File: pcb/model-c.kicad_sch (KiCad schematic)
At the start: 107 parts, among them IC1 HT16K33, IC2 HT16K33, J1 Batt, J2 Conn_01x02_Socket, SW1 SW_SPST, SW10 SW_SPST, SW11 SW_SPST, SW12 SW_SPST, SW13 SW_SPST, SW14 SW_SPST, SW15 SW_SPST, SW16 SW_SPST, SW17 SW_SPST, SW18 SW_SPST, SW19 SW_SPST, SW2 SW_SPST, SW20 SW_SPDT, SW3 SW_SPST, SW4 SW_SPST, SW5 SW_SPST, SW6 SW_SPST, SW7 SW_SPST, SW8 SW_SPST, SW9 SW_SPST, U1 W25Q16JVUXIQ, U2 14seg, U3 RP2040, U4 MCP73831-2-OT, U5 XC9140, U6 14seg, Y1 12MHz

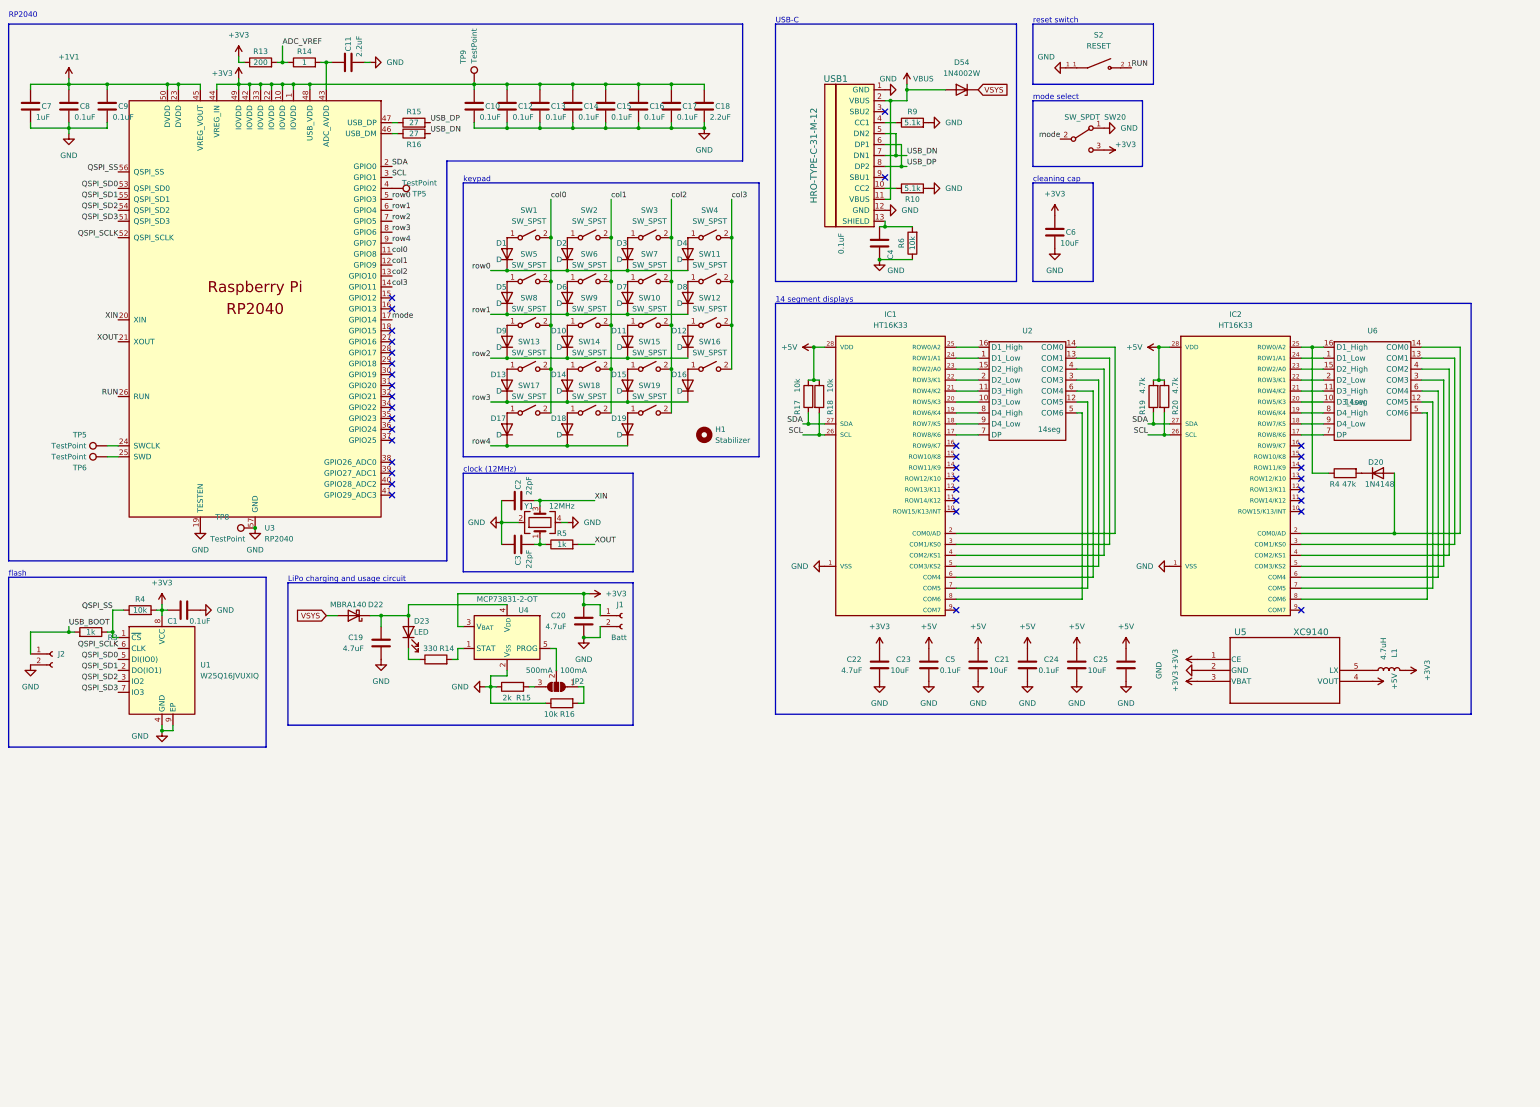
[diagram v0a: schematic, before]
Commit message: fixed power switch, mode button, updated readme, panelized, and added much better styling
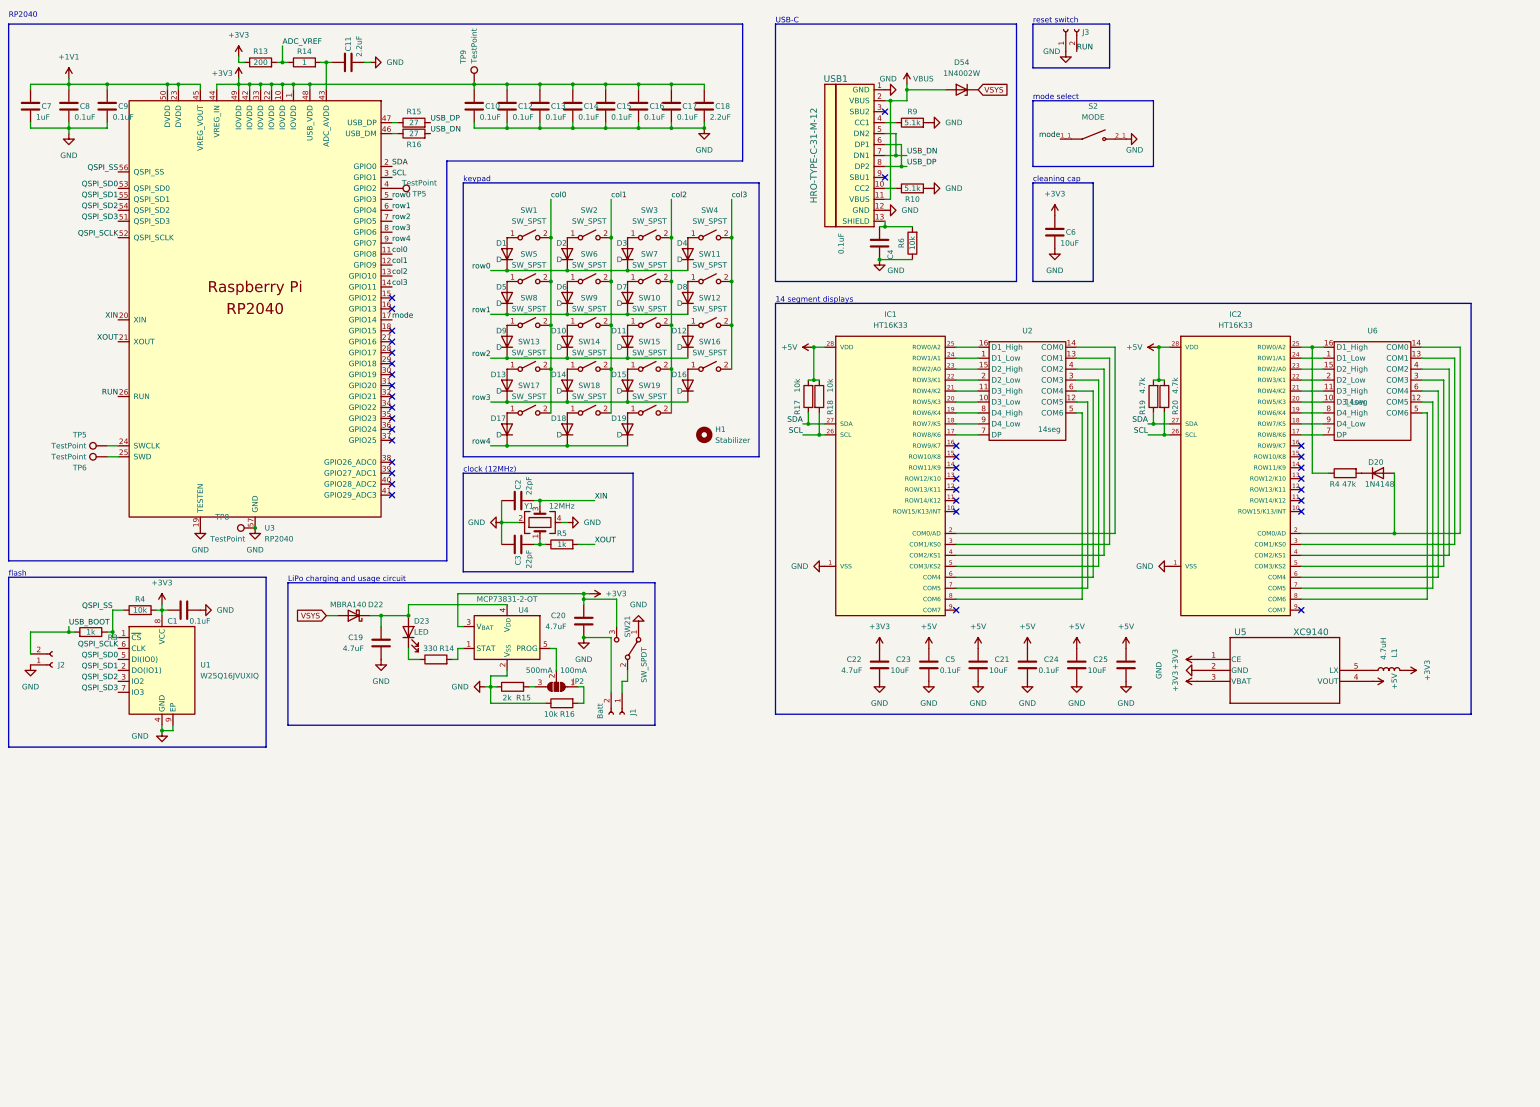
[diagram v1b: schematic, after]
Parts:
- removed SW20: SW_SPDT, footprints:MK-12C02-G020_GSW, symbol Switch:SW_SPDT
- added J3: Conn_01x02_Socket, Connector_PinSocket_2.54mm:PinSocket_1x02_P2.54mm_Vertical, symbol Connector:Conn_01x02_Socket
- added SW21: SW_SPDT, footprints:MK-12C02-G020_GSW, symbol Switch:SW_SPDT
- S2: value RESET -> MODE
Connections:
- net +3V3: now also SW21.3 (C); no longer J1.1 (Pin_1)
- net GND: now also J2.1 (Pin_1), S2.2_1, J3.1 (Pin_1), SW21.1 (A); no longer J2.2 (Pin_2), S2.1_1
- net RUN: now also J3.2 (Pin_2); no longer S2.2_1
- net USB_BOOT: now also J2.2 (Pin_2); no longer J2.1 (Pin_1)
- net mode: now also S2.1_1
- new net: J1.1 (Pin_1), SW21.2 (B)
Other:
- moved on the sheet: J1

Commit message: updating power system for automatic switching
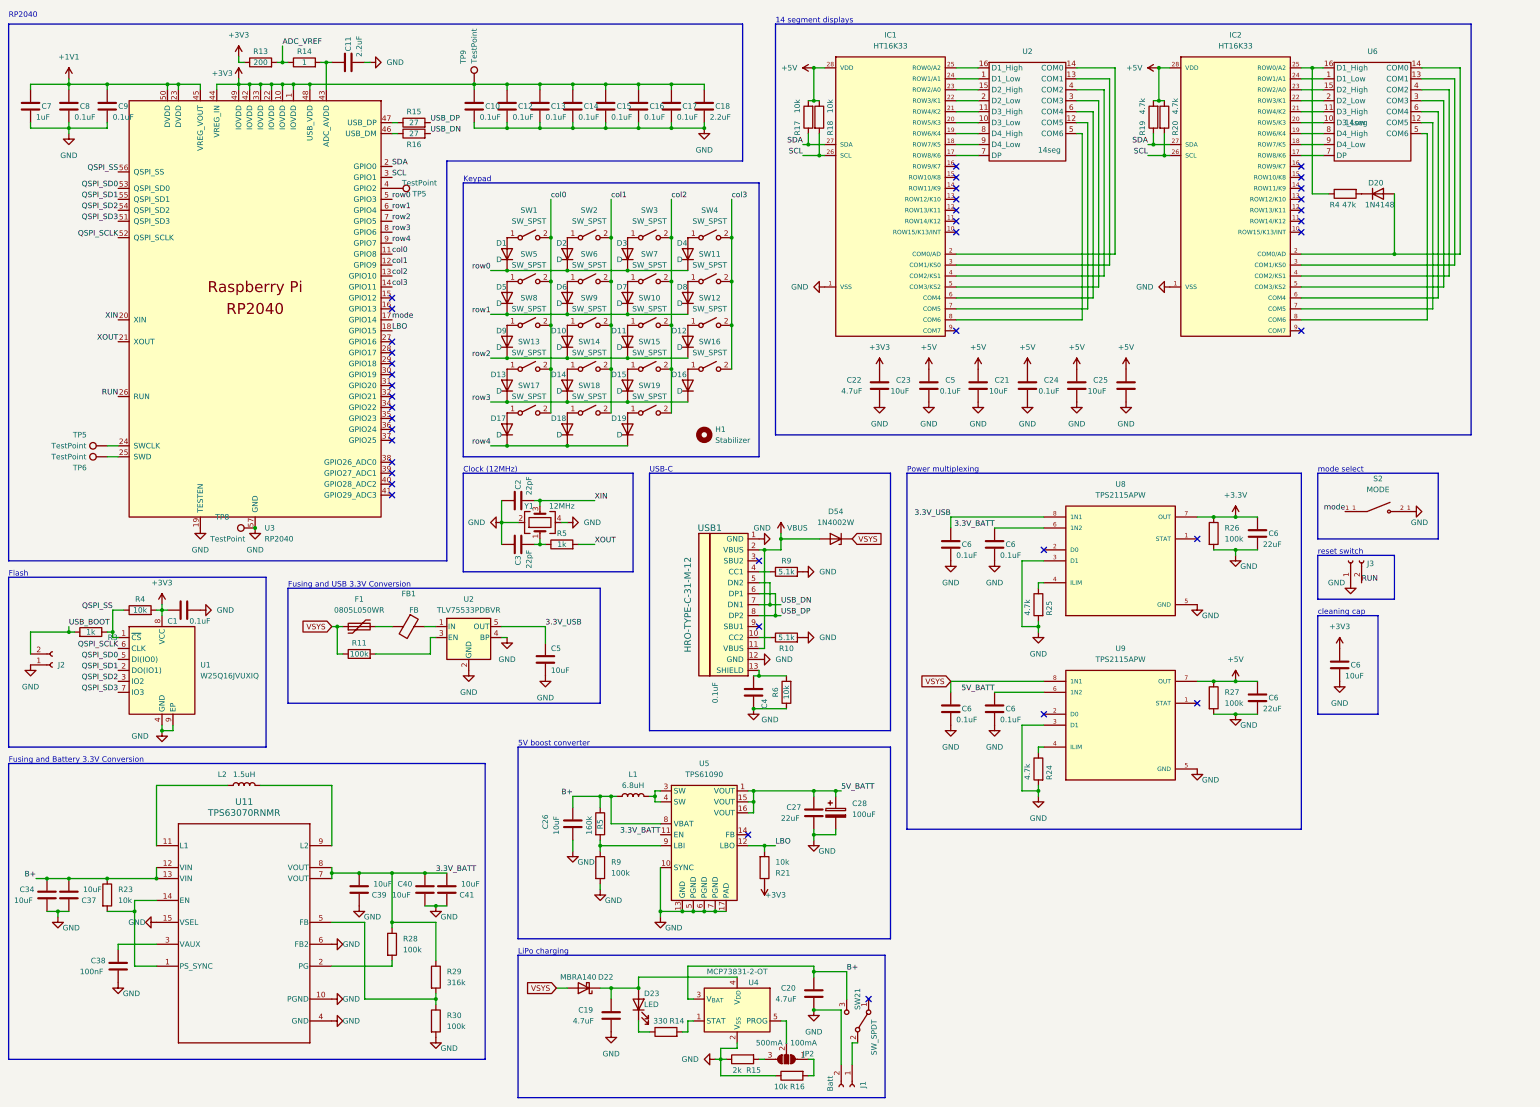
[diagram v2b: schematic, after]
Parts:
- removed U5: XC9140, footprints:GW_XC9140C501MR-G_TOR, symbol 2025-01-15_00-37-20:XC9140C501MR-G
- added C26, C34, C37, C39, C40, C41: 10uF, symbol Device:C
- added C27: 22uF, symbol Device:C
- added C28: 100uF, symbol Device:C_Polarized
- added C38: 100nF, symbol Device:C
- added C5: 10uF, Capacitor_SMD:C_0402_1005Metric, symbol Device:C
- added C6 (x4): 0.1uF, Capacitor_SMD:C_0402_1005Metric, symbol Device:C
- added C6 (x2): 22uF, Capacitor_SMD:C_0402_1005Metric, symbol Device:C
- added F1: 0805L050WR, Fuse:Fuse_0805_2012Metric, symbol Device:Polyfuse
- added FB1: FB, Resistor_SMD:R_0402_1005Metric, symbol Device:FerriteBead
- added L2: 1.5uH, symbol Device:L
- added R11: 100k, Resistor_SMD:R_0402_1005Metric, symbol Device:R
- added R21, R23: 10k, symbol Device:R
- added R24, R25: 4.7k, Resistor_SMD:R_0402_1005Metric, symbol Device:R
- added R26, R27, R28, R30, R9: 100k, symbol Device:R
- added R29: 316k, symbol Device:R
- added R5: 160k, symbol Device:R
- added U11: TPS63070RNMR, RNM0015A, symbol 2025-05-16_19-23-36:TPS63070RNMR
- added U2: TLV75533PDBVR, Package_TO_SOT_SMD:SOT-23-5, symbol Regulator_Linear:AP131-15
- added U5: TPS61090, Package_DFN_QFN:Texas_S-PVQFN-N16_EP2.7x2.7mm_ThermalVias, symbol Regulator_Switching:TPS61090
- added U8, U9: TPS2115APW, TPS2115APW:SOP65P640X120-8N, symbol TPS2115APW:TPS2115APW
- L1: value 4.7uH -> 6.8uH; footprint Inductor_SMD:L_TracoPower_TCK-047_5.2x5.8mm -> (none)
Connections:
- net +3V3: now also R21.1; no longer C20.1, L1.2, SW21.3 (C), U4.3 (V_{BAT})
- net +5V: now also C6.1, R27.1, U9.7 (OUT)
- net GND: now also C26.2, C27.2, C28.2, C34.2, C37.1, C38.2, C39.1, C40.2, C41.1, C5.2, C6.2, C6.2, C6.2, C6.2, C6.2, C6.2, R24.2, R25.2, R26.2, R27.2, R30.2, R9.2, U11.10 (PGND), U11.15 (VSEL), U11.4 (GND), U11.6 (FB2), U2.2 (GND), U2.4 (BP), U5.10 (SYNC), U5.13 (GND), U5.17 (PAD), U5.5 (PGND), U5.6 (PGND), U5.7 (PGND), U8.3 (D1), U8.5 (GND), U9.3 (D1), U9.5 (GND); no longer SW21.1 (A)
- net VSYS: now also C6.1, F1.1, R11.1, U9.8 (1N1)
- net B+: now reaches L1.1
- net B+: now also C20.1, SW21.3 (C), U4.3 (V_{BAT}), C26.1, C34.1, C37.2, R23.1, R5.1, U11.12 (VIN), U11.13 (VIN), U5.8 (VBAT)
- net LBO: now reaches U3.18 (GPIO15)
- net LBO: now also R21.2, U5.12 (LBO)
- new net: R29.2, R30.1, U11.5 (FB)
- new net: R5.2, R9.1, U5.9 (LBI)
- new net: C38.1, U11.3 (VAUX)
- new net: R24.1, U9.4 (ILIM)
- new net: FB1.1, U2.1 (IN)
- new net: F1.2, FB1.2
- new net: R25.1, U8.4 (ILIM)
- new net: R23.2, U11.1 (PS_SYNC), U11.14 (EN)
- new net: L2.1, U11.11 (L1)
- new net: R28.2, U11.2 (PG)
- new net: L2.2, U11.9 (L2)
- new net: R11.2, U2.3 (EN)
- new net: L1.2, U5.3 (SW), U5.4 (SW)
- new net +3.3V: C6.1, R26.1, U8.7 (OUT)
- new net 3.3V_BATT: C39.2, C40.1, C41.2, C6.1, R28.1, R29.1, U11.7 (VOUT), U11.8 (VOUT), U5.11 (EN), U8.6 (1N2)
- new net 3.3V_USB: C5.1, C6.1, U2.5 (OUT), U8.8 (1N1)
- new net 5V_BATT: C27.1, C28.1, C6.1, U5.1 (VOUT), U5.15 (VOUT), U5.16 (VOUT), U9.6 (1N2)
- no-connect marks 35 -> 40
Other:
- note added: "5V boost converter"
- note added: "Clock (12MHz)"
- note added: "Flash"
- note added: "Fusing and Battery 3.3V Conversion"
- note added: "Fusing and USB 3.3V Conversion"
- note added: "Keypad"
- note added: "LiPo charging"
- note added: "Power multiplexing"
- note removed: "LiPo charging and usage circuit"
- note removed: "clock (12MHz)"
- note removed: "flash"
- note removed: "keypad"
- moved on the sheet: C19, C20, C21, C22, C23, C24, C25, C4, C5, C6, D20, D22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
